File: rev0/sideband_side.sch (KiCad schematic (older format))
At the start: 18 parts, among them IC1 ECP5-BGA256, U8 USB3343

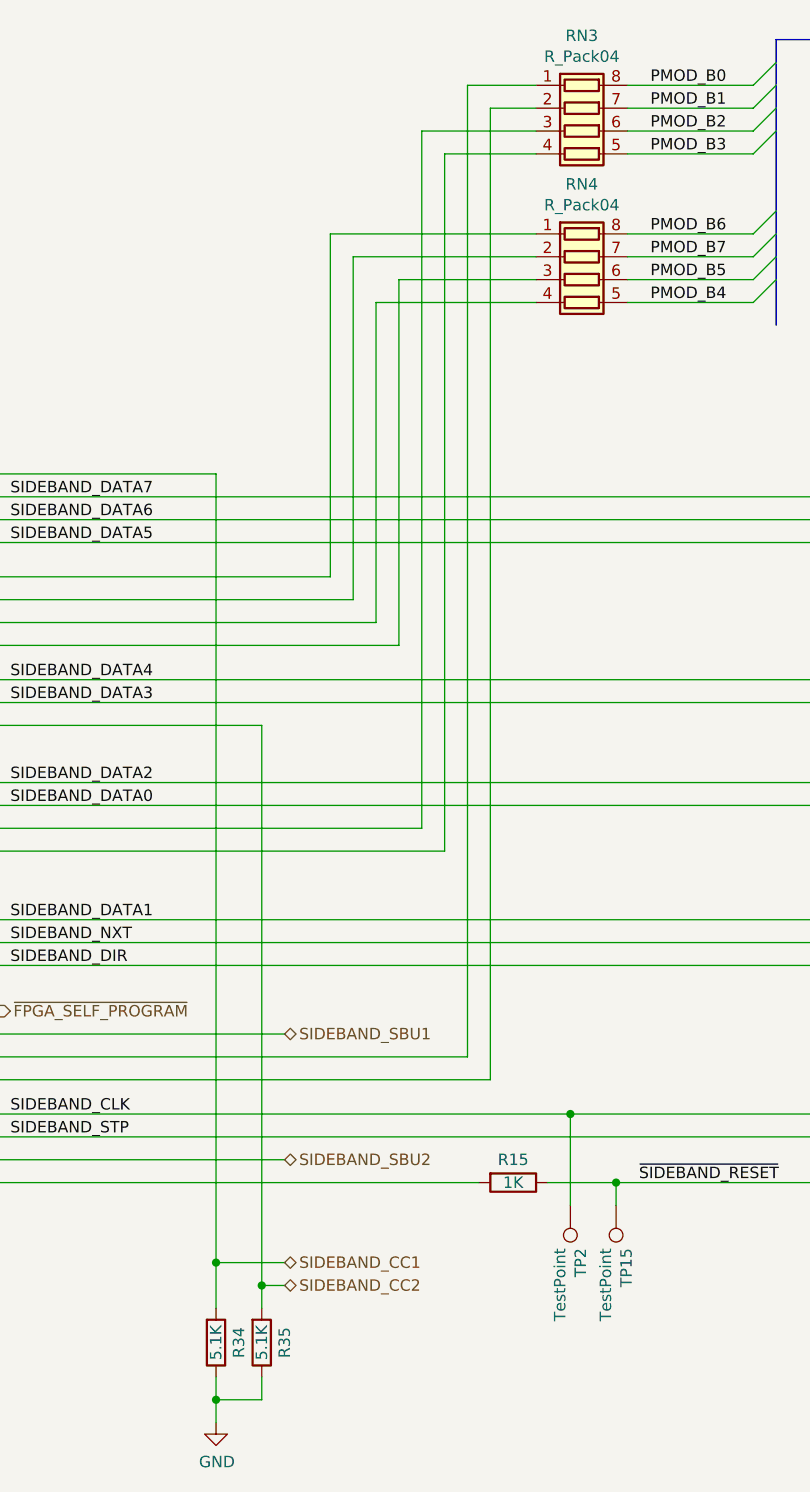
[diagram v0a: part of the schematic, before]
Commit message: hardware: clarify schematic
specify CC resistors as ±10% to hint that the spec requires it
add resistance value to resistor networks
give UART nets top-level names indicating JTAG functions
change AP22811 values to AP22811A
change PMOD to Pmod
nudge FPGA_TMS trace to make it more bodgeable
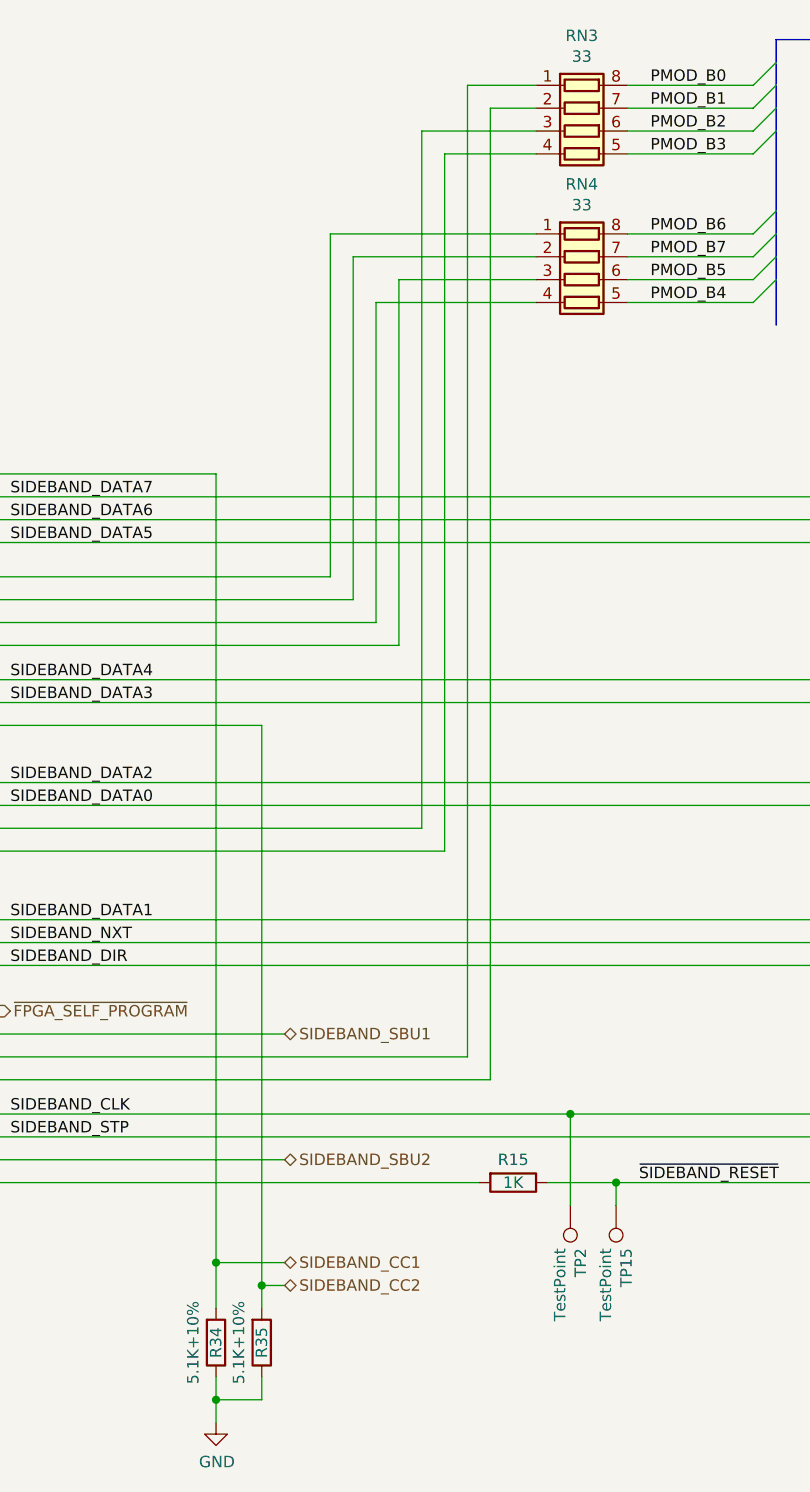
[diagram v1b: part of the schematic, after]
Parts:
- R34, R35: value 5.1K -> 5.1K+10%
- RN3, RN4: value R_Pack04 -> 33
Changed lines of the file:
@@
 Sheet 2 9
 Title "LUNA: Sideband USB PHY"
-Date "2021-01-05"
+Date "2021-01-08"
 Rev "r0"
 Comp "Copyright 2019-2021 Great Scott Gadgets"
@@
 AR Path="/5DD754D4/60996F81" Ref="R?"  Part="1"
 AR Path="/5DCD9772/60996F81" Ref="R34"  Part="1"
-F 0 "R34" V 3500 6900 50  0000 C CNN
-F 1 "5.1K" V 3400 6900 50  0000 C CNN
+F 0 "R34" V 3400 6900 50  0000 C CNN
+F 1 "5.1K+10%" V 3300 6900 50  0000 C CNN
 F 2 "Resistor_SMD:R_0402_1005Metric" V 3330 6900 50  0001 C CNN
 F 3 "~" H 3400 6900 50  0001 C CNN
@@
 AR Path="/5DD754D4/60996F8E" Ref="R?"  Part="1"
 AR Path="/5DCD9772/60996F8E" Ref="R35"  Part="1"
-F 0 "R35" V 3700 6900 50  0000 C CNN
-F 1 "5.1K" V 3600 6900 50  0000 C CNN
+F 0 "R35" V 3600 6900 50  0000 C CNN
+F 1 "5.1K+10%" V 3500 6900 50  0000 C CNN
 F 2 "Resistor_SMD:R_0402_1005Metric" V 3530 6900 50  0001 C CNN
 F 3 "~" H 3600 6900 50  0001 C CNN
@@
 AR Path="/5DCD9772/60DD013F" Ref="RN3"  Part="1"
 F 0 "RN3" V 4583 1600 50  0000 C CNN
-F 1 "R_Pack04" V 4674 1600 50  0000 C CNN
+F 1 "33" V 4674 1600 50  0000 C CNN
 F 2 "Resistor_SMD:R_Array_Convex_4x0402" V 5275 1600 50  0001 C CNN
 F 3 "~" H 5000 1600 50  0001 C CNN
@@
 AR Path="/5DCD9772/60DD0149" Ref="RN4"  Part="1"
 F 0 "RN4" V 4583 2250 50  0000 C CNN
-F 1 "R_Pack04" V 4674 2250 50  0000 C CNN
+F 1 "33" V 4674 2250 50  0000 C CNN
 F 2 "Resistor_SMD:R_Array_Convex_4x0402" V 5275 2250 50  0001 C CNN
 F 3 "~" H 5000 2250 50  0001 C CNN

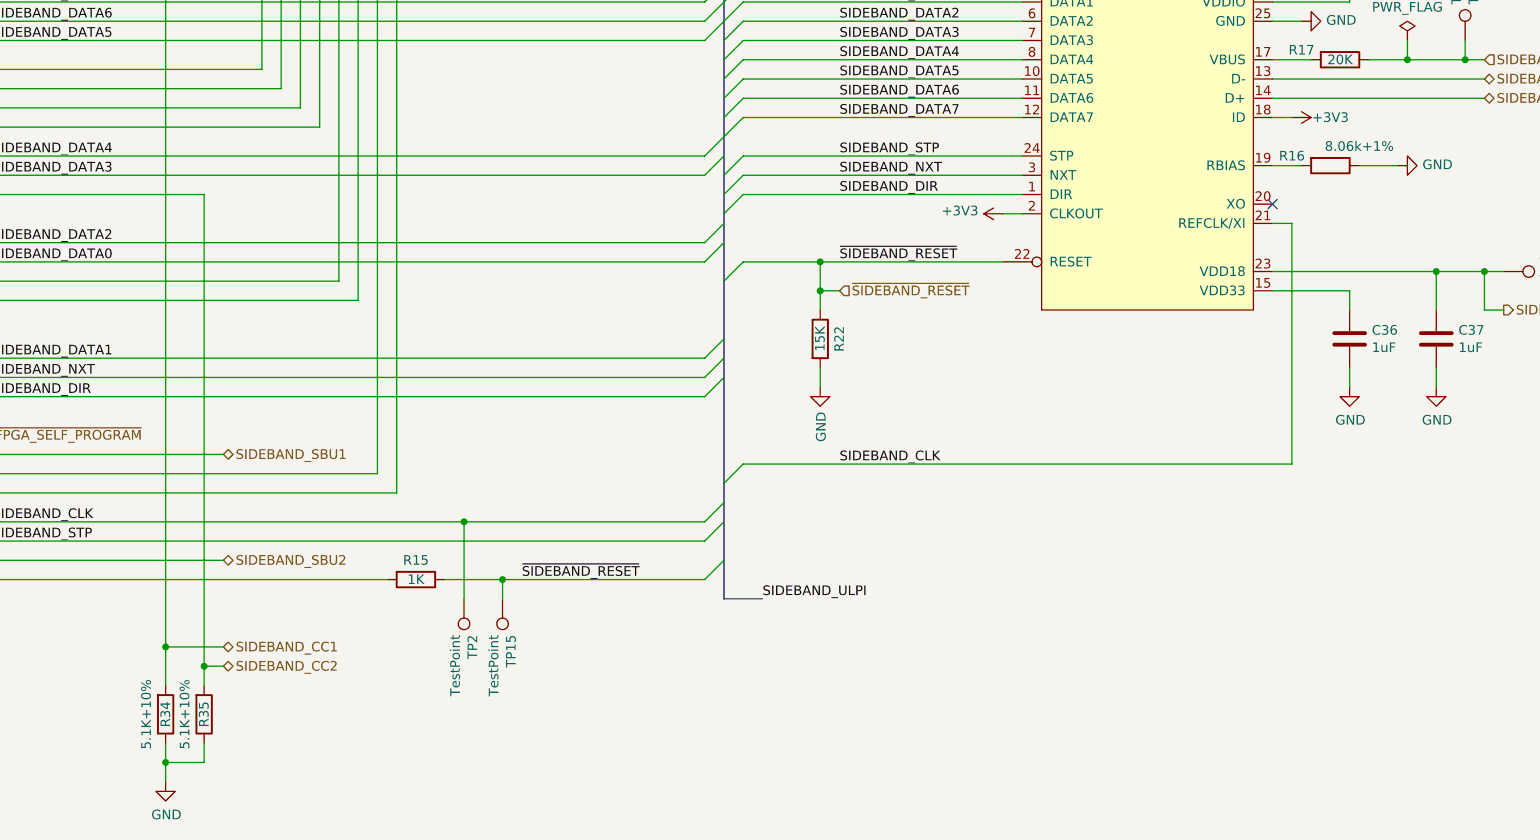
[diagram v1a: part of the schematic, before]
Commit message: hardware: select LEDs and series resistors
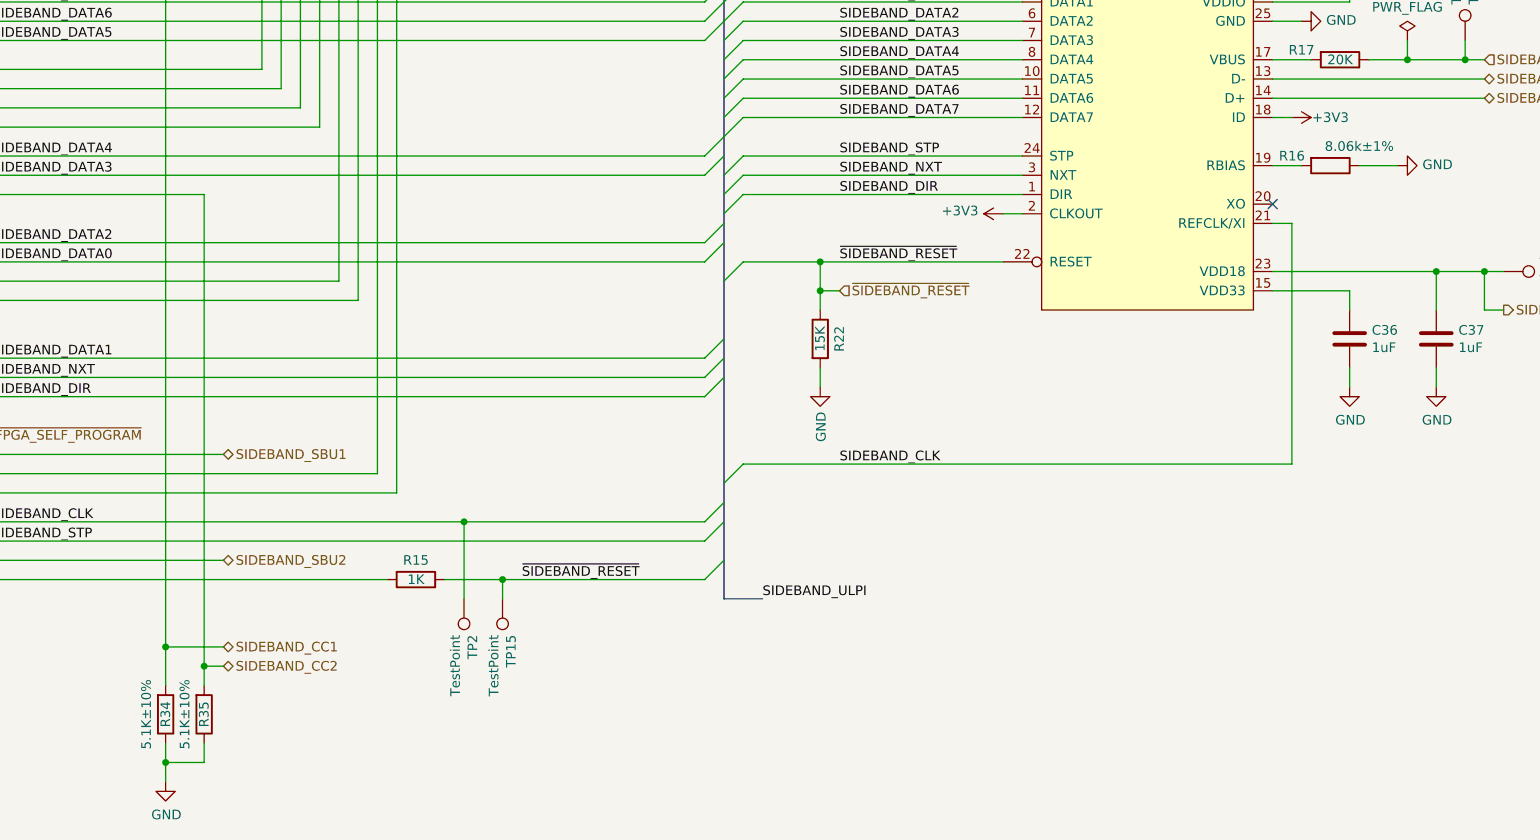
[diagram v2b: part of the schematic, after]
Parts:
- R16: value 8.06k+1% -> 8.06k±1%
- R34, R35: value 5.1K+10% -> 5.1K±10%
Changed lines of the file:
@@
 Sheet 2 9
 Title "LUNA: Sideband USB PHY"
-Date "2021-01-08"
+Date "2021-01-10"
 Rev "r0"
 Comp "Copyright 2019-2021 Great Scott Gadgets"
@@
 AR Path="/5DCD9772/60996F81" Ref="R34"  Part="1"
 F 0 "R34" V 3400 6900 50  0000 C CNN
-F 1 "5.1K+10%" V 3300 6900 50  0000 C CNN
+F 1 "5.1K±10%" V 3300 6900 50  0000 C CNN
 F 2 "Resistor_SMD:R_0402_1005Metric" V 3330 6900 50  0001 C CNN
 F 3 "~" H 3400 6900 50  0001 C CNN
@@
 AR Path="/5DCD9772/60996F8E" Ref="R35"  Part="1"
 F 0 "R35" V 3600 6900 50  0000 C CNN
-F 1 "5.1K+10%" V 3500 6900 50  0000 C CNN
+F 1 "5.1K±10%" V 3500 6900 50  0000 C CNN
 F 2 "Resistor_SMD:R_0402_1005Metric" V 3530 6900 50  0001 C CNN
 F 3 "~" H 3600 6900 50  0001 C CNN
@@
 P 9450 4050
 F 0 "R16" V 9400 3850 50  0000 C CNN
-F 1 "8.06k+1%" V 9350 4200 50  0000 C CNN
+F 1 "8.06k±1%" V 9350 4200 50  0000 C CNN
 F 2 "Resistor_SMD:R_0402_1005Metric" V 9380 4050 50  0001 C CNN
 F 3 "~" H 9450 4050 50  0001 C CNN

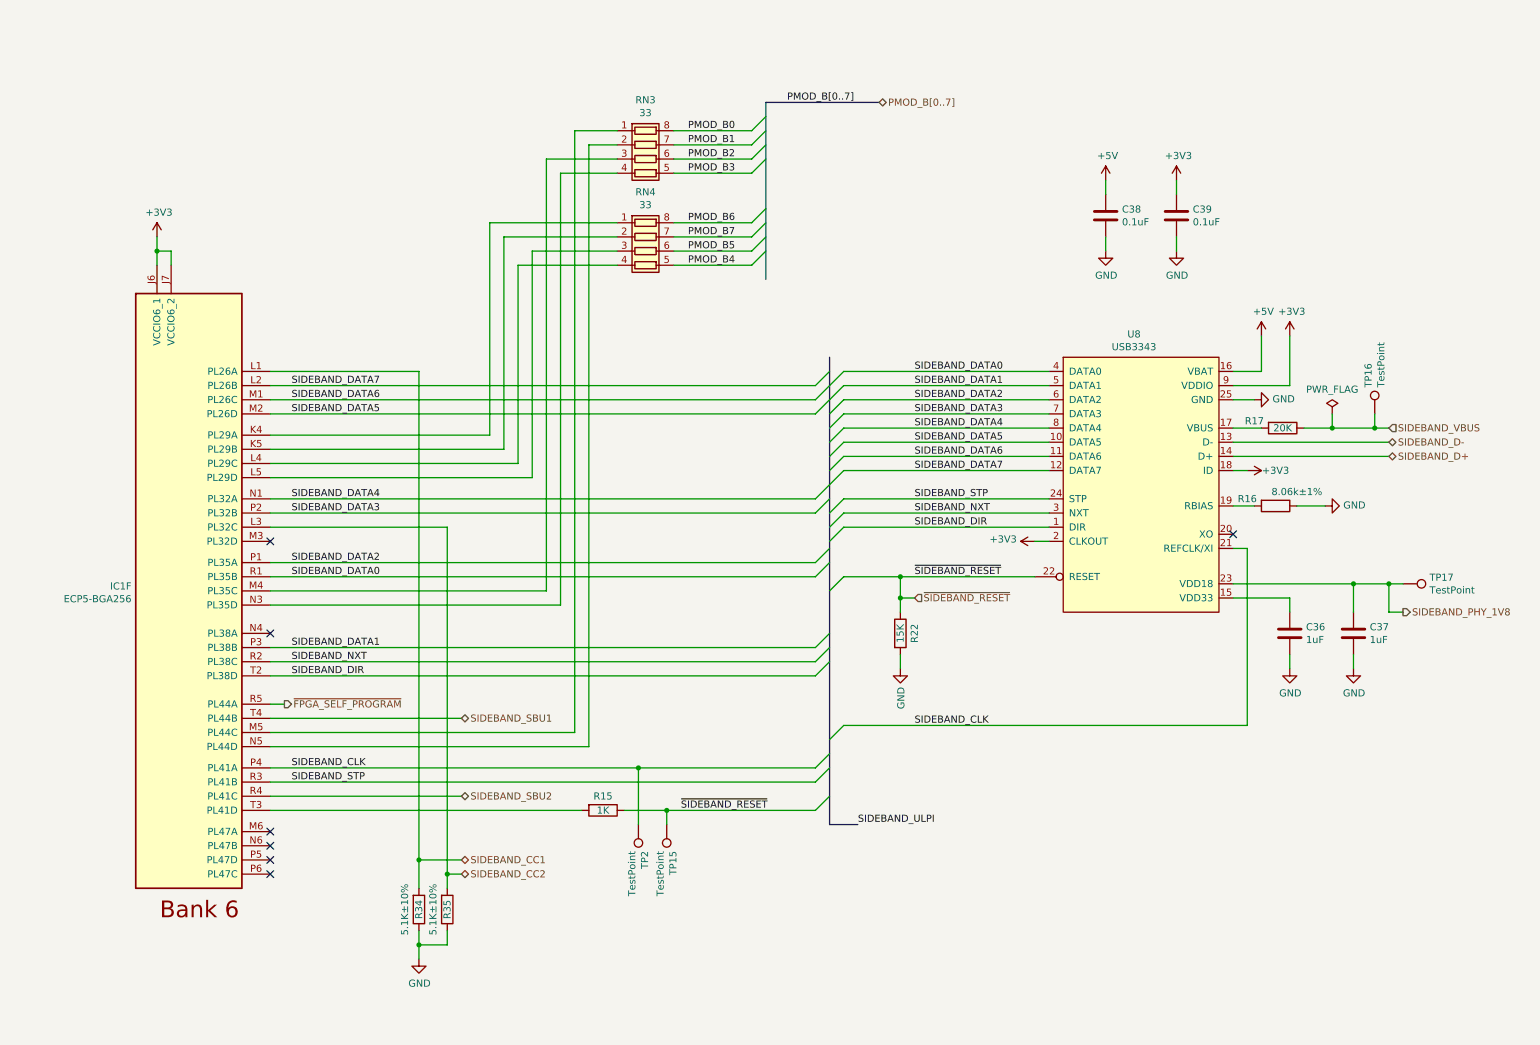
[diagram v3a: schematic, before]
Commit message: hardware: add optional capacitors to some user i/o
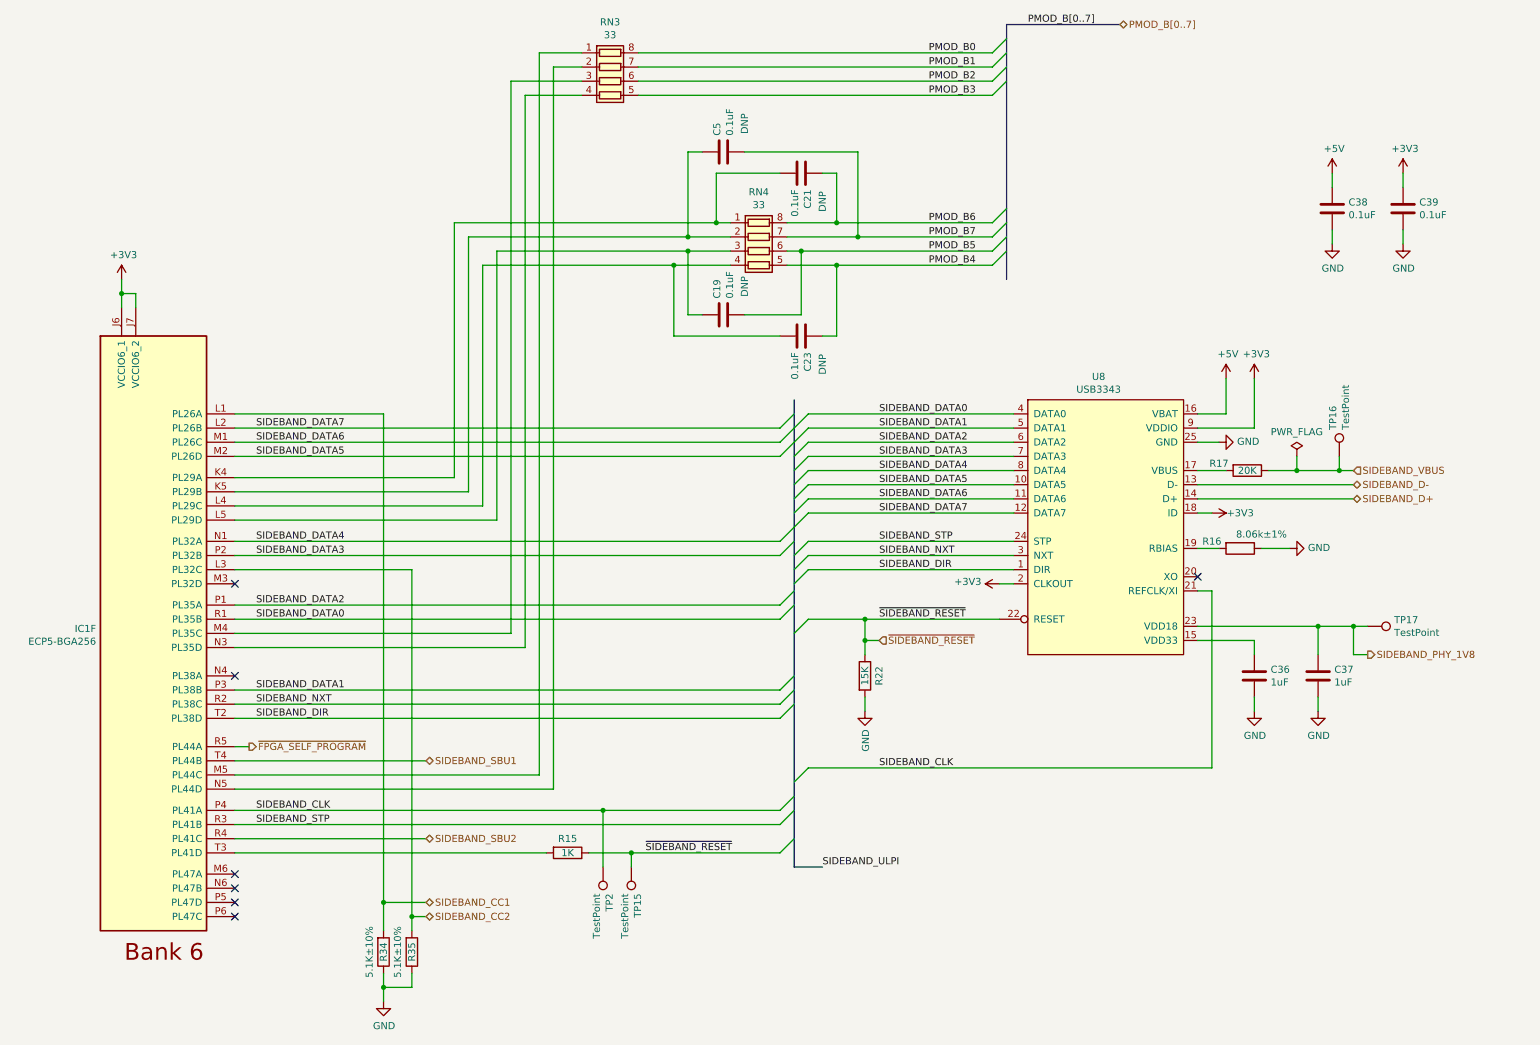
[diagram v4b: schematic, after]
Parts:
- added C19, C21, C23, C5: 0.1uF, Capacitor_SMD:C_0402_1005Metric, symbol Device:C
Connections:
- net PMOD_B4: now also C23.1
- net PMOD_B5: now also C19.2
- net PMOD_B6: now also C21.1
- net PMOD_B7: now also C5.2
- net at IC1.K4 (PL29A), RN4.1 (R1.1): now also C21.2
- net at IC1.K5 (PL29B), RN4.2 (R2.1): now also C5.1
- net at IC1.L4 (PL29C), RN4.4 (R4.1): now also C23.2
- net at IC1.L5 (PL29D), RN4.3 (R3.1): now also C19.1
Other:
- moved on the sheet: C36, C37, C38, C39, IC1F, R15, R16, R17, R22, R34, R35, RN3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
